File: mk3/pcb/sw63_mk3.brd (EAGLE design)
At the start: 35 x 35 mm, 65 parts, among them J1 USB-C_2.0_SMT, Q1 LGE2305, Q2 BC817S, Q3 BC817S, Q4 TEMT6200FX01, SW1 KSC321JLFS, SW2 EVQ-P7J01P, U1 ATSAMD21E18A-MU, U2 DS3231MZ+, U3 TLC5916IPW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

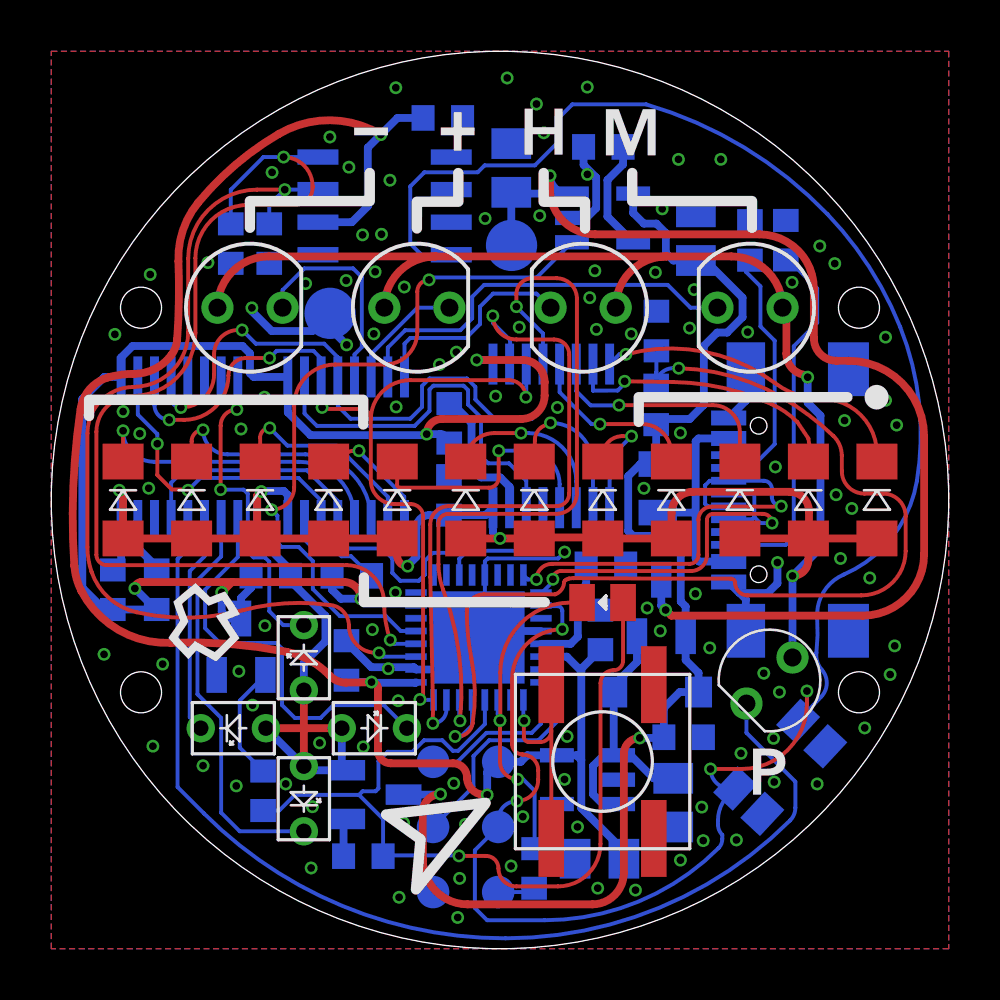
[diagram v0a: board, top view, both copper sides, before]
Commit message: layout changes for better case compatibility
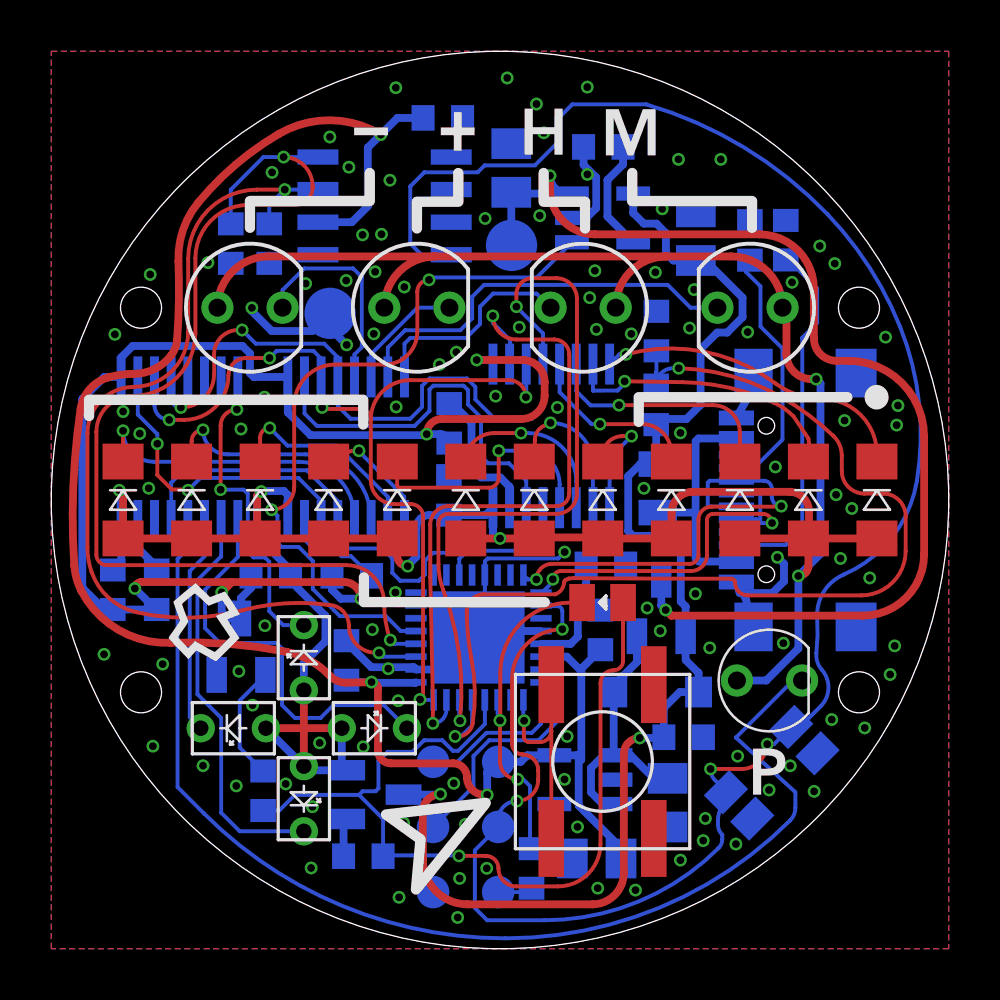
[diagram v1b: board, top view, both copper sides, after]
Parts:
- moved SW2 0.39 mm to (28.1, 6.86), turned to 315 degrees
- moved J1 0.30 mm to (30.3, 17.5)
- moved C3 0.22 mm to (24.0, 5.70)
- moved C4 0.11 mm to (21.3, 3.52)
- moved U6 0.10 mm to (20.8, 6.59)
- moved R14 0.10 mm to (18.7, 3.13)
- turned PM to 0 degrees
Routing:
- net !RESET: track 81.1 -> 78.5 mm
- net VDDLEDS: track 115.5 -> 118.0 mm
- net N$15: track 42.1 -> 44.6 mm
- net N$1: track 8.74 -> 9.34 mm
- net GND: track 32.5 -> 32.2 mm, vias 109 -> 108

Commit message: update led colors to match reality
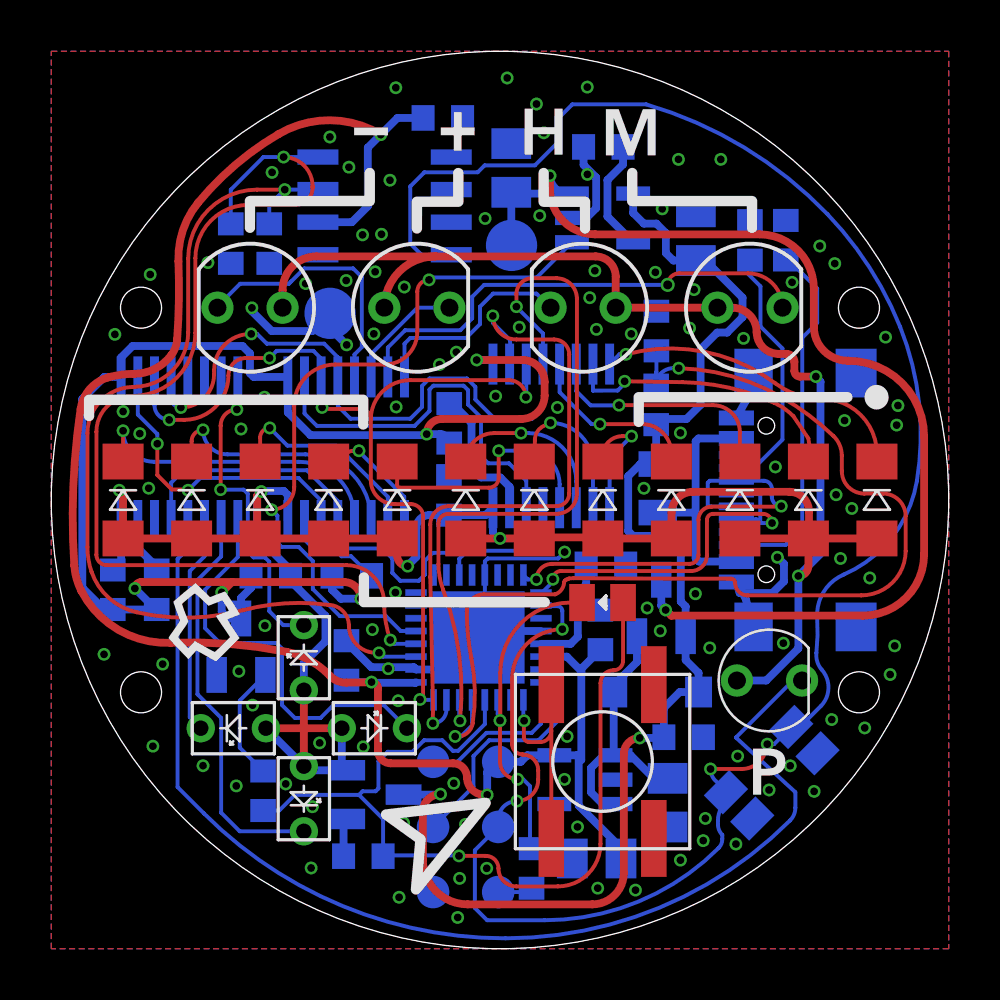
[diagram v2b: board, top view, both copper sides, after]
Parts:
- HOURS: device BASTL_LEDS:LED_5MM_ALT -> BASTL_LEDS:LED_5MM_BLUE
- MINUS: device BASTL_LEDS:LED_5MM_ALT -> BASTL_LEDS:LED_5MM_RED
- MINUTES: device BASTL_LEDS:LED_5MM_ALT -> BASTL_LEDS:LED_5MM_YELLOW
- PLUS: device BASTL_LEDS:LED_5MM_ALT -> BASTL_LEDS:LED_5MM_GREEN
- moved MINUS 6.51 mm to (7.75, 25.0), turned to 180 degrees
- moved PLUS 6.51 mm to (14.3, 25.0)
- turned MINUTES to 0 degrees
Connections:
- net N$33: now also PLUS.K; no longer MINUS.K
- net N$34: now also MINUS.K; no longer PLUS.K
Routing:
- net VDDLEDS: track 118.0 -> 113.0 mm
- net N$32: track 15.9 -> 18.8 mm, vias 0 -> 1
- net N$34: track 8.28 -> 10.4 mm
